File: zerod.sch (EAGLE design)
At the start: 38 parts, among them IC1 NE5532N, IC2 LM3914N, Q1 2N3906

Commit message: new, smaller board
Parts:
- renumbered C2 to C3, CY2 to C6
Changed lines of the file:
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@@
 <grid distance="0.1" unitdist="inch" unit="inch" style="lines" multiple="1" display="no" altdistance="0.01" altunitdist="inch" altunit="inch"/>
 <layers>
-<layer number="1" name="Top" color="4" fill="1" visible="yes" active="no"/>
-<layer number="16" name="Bottom" color="1" fill="1" visible="yes" active="no"/>
-<layer number="17" name="Pads" color="2" fill="1" visible="yes" active="no"/>
-<layer number="18" name="Vias" color="2" fill="1" visible="yes" active="no"/>
-<layer number="19" name="Unrouted" color="6" fill="1" visible="yes" active="no"/>
-<layer number="20" name="Dimension" color="15" fill="1" visible="yes" active="no"/>
-<layer number="21" name="tPlace" color="7" fill="1" visible="yes" active="no"/>
-<layer number="22" name="bPlace" color="7" fill="1" visible="yes" active="no"/>
-<layer number="23" name="tOrigins" color="15" fill="1" visible="yes" active="no"/>
-<layer number="24" name="bOrigins" color="15" fill="1" visible="yes" active="no"/>
-<layer number="25" name="tNames" color="7" fill="1" visible="yes" active="no"/>
-<layer number="26" name="bNames" color="7" fill="1" visible="yes" active="no"/>
-<layer number="27" name="tValues" color="7" fill="1" visible="yes" active="no"/>
-<layer number="28" name="bValues" color="7" fill="1" visible="yes" active="no"/>
+<layer number="1" name="Top" color="4" fill="1" visible="no" active="no"/>
+<layer number="16" name="Bottom" color="1" fill="1" visible="no" active="no"/>
+<layer number="17" name="Pads" color="2" fill="1" visible="no" active="no"/>
+<layer number="18" name="Vias" color="2" fill="1" visible="no" active="no"/>
+<layer number="19" name="Unrouted" color="6" fill="1" visible="no" active="no"/>
+<layer number="20" name="Dimension" color="15" fill="1" visible="no" active="no"/>
+<layer number="21" name="tPlace" color="7" fill="1" visible="no" active="no"/>
+<layer number="22" name="bPlace" color="7" fill="1" visible="no" active="no"/>
+<layer number="23" name="tOrigins" color="15" fill="1" visible="no" active="no"/>
+<layer number="24" name="bOrigins" color="15" fill="1" visible="no" active="no"/>
+<layer number="25" name="tNames" color="7" fill="1" visible="no" active="no"/>
+<layer number="26" name="bNames" color="7" fill="1" visible="no" active="no"/>
+<layer number="27" name="tValues" color="7" fill="1" visible="no" active="no"/>
+<layer number="28" name="bValues" color="7" fill="1" visible="no" active="no"/>
 <layer number="29" name="tStop" color="7" fill="3" visible="no" active="no"/>
 <layer number="30" name="bStop" color="7" fill="6" visible="no" active="no"/>
@@
 <layer number="35" name="tGlue" color="7" fill="4" visible="no" active="no"/>
 <layer number="36" name="bGlue" color="7" fill="5" visible="no" active="no"/>
-<layer number="37" name="tTest" color="7" fill="1" visible="yes" active="no"/>
-<layer number="38" name="bTest" color="7" fill="1" visible="yes" active="no"/>
+<layer number="37" name="tTest" color="7" fill="1" visible="no" active="no"/>
+<layer number="38" name="bTest" color="7" fill="1" visible="no" active="no"/>
 <layer number="39" name="tKeepout" color="4" fill="11" visible="no" active="no"/>
 <layer number="40" name="bKeepout" color="1" fill="11" visible="no" active="no"/>
@@
 <layer number="44" name="Drills" color="7" fill="1" visible="no" active="no"/>
 <layer number="45" name="Holes" color="7" fill="1" visible="no" active="no"/>
-<layer number="46" name="Milling" color="3" fill="1" visible="yes" active="no"/>
-<layer number="47" name="Measures" color="7" fill="1" visible="yes" active="no"/>
-<layer number="48" name="Document" color="7" fill="1" visible="yes" active="no"/>
-<layer number="49" name="Reference" color="7" fill="1" visible="yes" active="no"/>
-<layer number="50" name="dxf" color="7" fill="1" visible="yes" active="no"/>
-<layer number="51" name="tDocu" color="7" fill="1" visible="yes" active="no"/>
-<layer number="52" name="bDocu" color="7" fill="1" visible="yes" active="no"/>
-<layer number="53" name="tGND_GNDA" color="7" fill="9" visible="yes" active="no"/>
-<layer number="54" name="bGND_GNDA" color="1" fill="9" visible="yes" active="no"/>
-<layer number="56" name="wert" color="7" fill="1" visible="yes" active="no"/>
+<layer number="46" name="Milling" color="3" fill="1" visible="no" active="no"/>
+<layer number="47" name="Measures" color="7" fill="1" visible="no" active="no"/>
+<layer number="48" name="Document" color="7" fill="1" visible="no" active="no"/>
+<layer number="49" name="Reference" color="7" fill="1" visible="no" active="no"/>
+<layer number="50" name="dxf" color="7" fill="1" visible="no" active="no"/>
+<layer number="51" name="tDocu" color="7" fill="1" visible="no" active="no"/>
+<layer number="52" name="bDocu" color="7" fill="1" visible="no" active="no"/>
+<layer number="53" name="tGND_GNDA" color="7" fill="9" visible="no" active="no"/>
+<layer number="54" name="bGND_GNDA" color="1" fill="9" visible="no" active="no"/>
+<layer number="56" name="wert" color="7" fill="1" visible="no" active="no"/>
 <layer number="90" name="Modules" color="5" fill="1" visible="yes" active="yes"/>
 <layer number="91" name="Nets" color="2" fill="1" visible="yes" active="yes"/>
@@
 <part name="R12" library="rcl" deviceset="POTENTIOMETER_" device="PT-10S" value="5k"/>
 <part name="GND5" library="supply1" deviceset="GNDA" device=""/>
-<part name="CY2" library="rcl" deviceset="CPOL-US" device="E22-6AXIAL" value="10uF"/>
 <part name="GND7" library="supply1" deviceset="GNDA" device=""/>
 <part name="GND8" library="supply1" deviceset="GNDA" device=""/>
@@
 <part name="R3" library="rcl" deviceset="R-US_" device="0207/10" value="1k"/>
 <part name="CY3" library="rcl" deviceset="CY" device="YC7B5" value="470pF"/>
-<part name="C2" library="rcl" deviceset="CPOL-US" device="E22-6AXIAL" value="100uF"/>
 <part name="R4" library="bourns" deviceset="91" device="" value="5k"/>
 <part name="GND3" library="supply1" deviceset="GNDA" device=""/>
@@
 <part name="D2" library="diode" deviceset="1N5908" device=""/>
 <part name="D3" library="diode" deviceset="1N5908" device=""/>
+<part name="C3" library="rcl" deviceset="CPOL-US" device="E22-6AXIAL" value="100uF"/>
+<part name="C6" library="rcl" deviceset="CPOL-US" device="E22-6AXIAL" value="10uF"/>
 </parts>
 <sheets>
@@
 <instance part="R12" gate="1" x="91.44" y="12.7" rot="R90"/>
 <instance part="GND5" gate="1" x="91.44" y="-7.62"/>
-<instance part="CY2" gate="G$1" x="137.16" y="2.54"/>
 <instance part="GND7" gate="1" x="109.22" y="-7.62"/>
 <instance part="GND8" gate="1" x="137.16" y="-7.62"/>
@@
 <instance part="R3" gate="G$1" x="38.1" y="68.58" rot="R180"/>
 <instance part="CY3" gate="G$1" x="48.26" y="60.96"/>
-<instance part="C2" gate="G$1" x="83.82" y="71.12" rot="R90"/>
 <instance part="R4" gate="G$1" x="27.94" y="68.58"/>
 <instance part="IC1" gate="B" x="7.62" y="58.42"/>
@@
 <instance part="D2" gate="1" x="7.62" y="35.56" rot="R90"/>
 <instance part="D3" gate="1" x="7.62" y="22.86" rot="R90"/>
+<instance part="C3" gate="G$1" x="83.82" y="71.12" rot="R90"/>
+<instance part="C6" gate="G$1" x="137.16" y="2.54"/>
 </instances>
 <busses>
@@
 </segment>
 <segment>
-<pinref part="CY2" gate="G$1" pin="-"/>
 <pinref part="GND8" gate="1" pin="GNDA"/>
 <wire x1="137.16" y1="-2.54" x2="137.16" y2="-5.08" width="0.1524" layer="91"/>
+<pinref part="C6" gate="G$1" pin="-"/>
 </segment>
 <segment>
@@
 <wire x1="58.42" y1="83.82" x2="76.2" y2="83.82" width="0.1524" layer="91"/>
 <wire x1="76.2" y1="45.72" x2="76.2" y2="71.12" width="0.1524" layer="91"/>
-<pinref part="C2" gate="G$1" pin="+"/>
 <wire x1="76.2" y1="71.12" x2="81.28" y2="71.12" width="0.1524" layer="91"/>
+<pinref part="C3" gate="G$1" pin="+"/>
 </segment>
 </net>
@@
 <wire x1="121.92" y1="48.26" x2="121.92" y2="45.72" width="0.1524" layer="91"/>
 <wire x1="121.92" y1="45.72" x2="137.16" y2="45.72" width="0.1524" layer="91"/>
-<pinref part="CY2" gate="G$1" pin="+"/>
 <wire x1="137.16" y1="45.72" x2="137.16" y2="7.62" width="0.1524" layer="91"/>
 <pinref part="IC2" gate="A" pin="V+"/>
@@
 <wire x1="109.22" y1="45.72" x2="121.92" y2="45.72" width="0.1524" layer="91"/>
 <junction x="121.92" y="45.72"/>
+<pinref part="C6" gate="G$1" pin="+"/>
 </segment>
 <segment>
@@
 <net name="N$3" class="0">
 <segment>
-<pinref part="C2" gate="G$1" pin="-"/>
 <pinref part="R15" gate="G$1" pin="1"/>
 <wire x1="88.9" y1="71.12" x2="93.98" y2="71.12" width="0.1524" layer="91"/>
-</segment>
-</net>
+<pinref part="C3" gate="G$1" pin="-"/>
+</segment>
+</net>

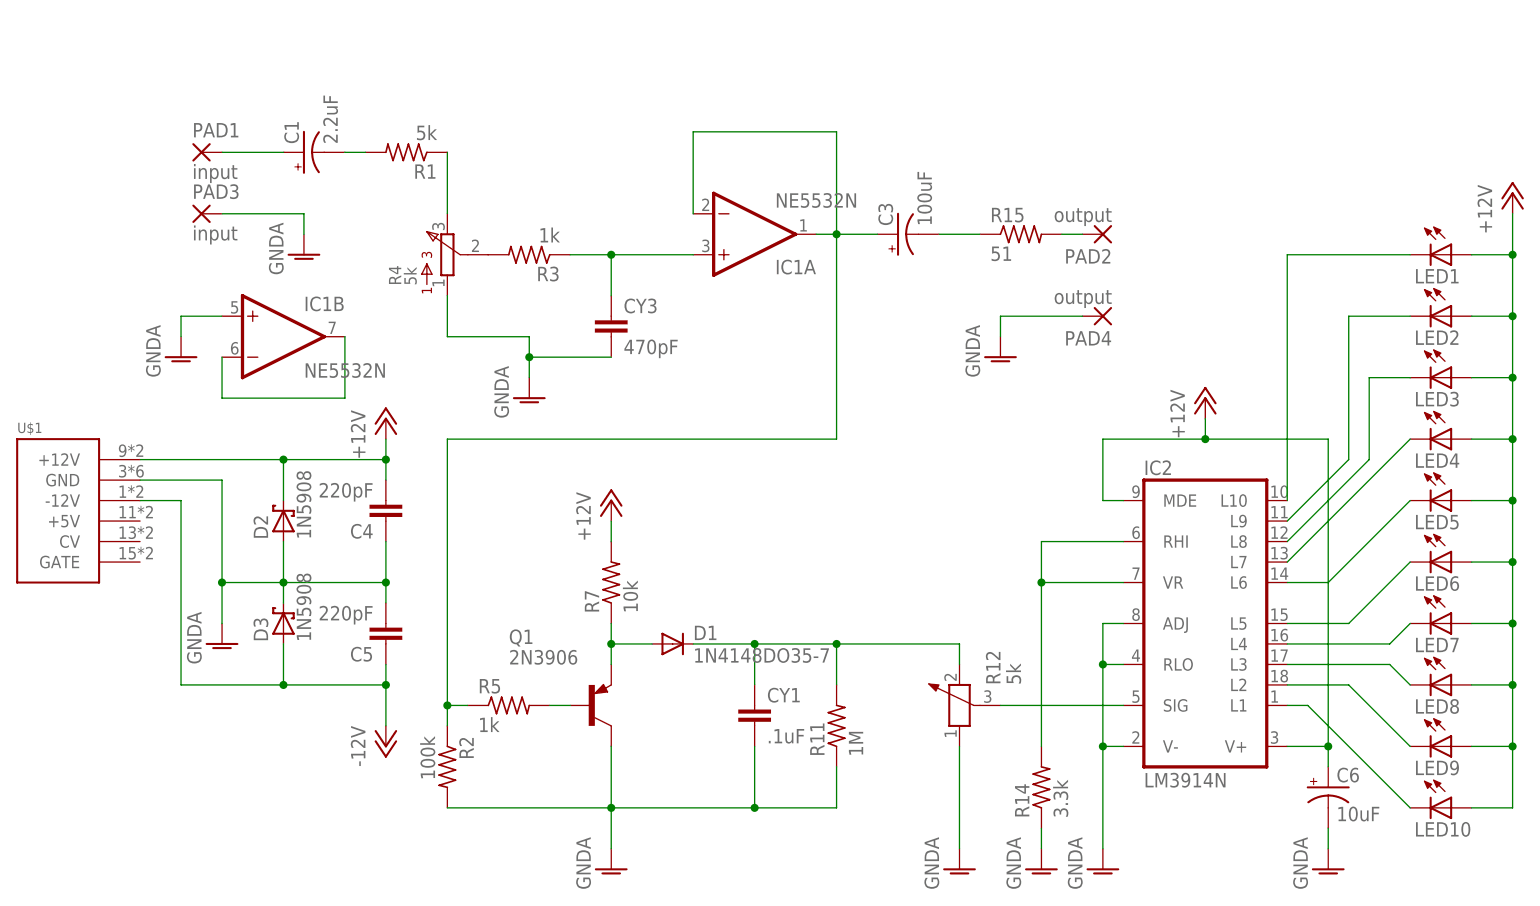
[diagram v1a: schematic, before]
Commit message: trimmer before peak detector
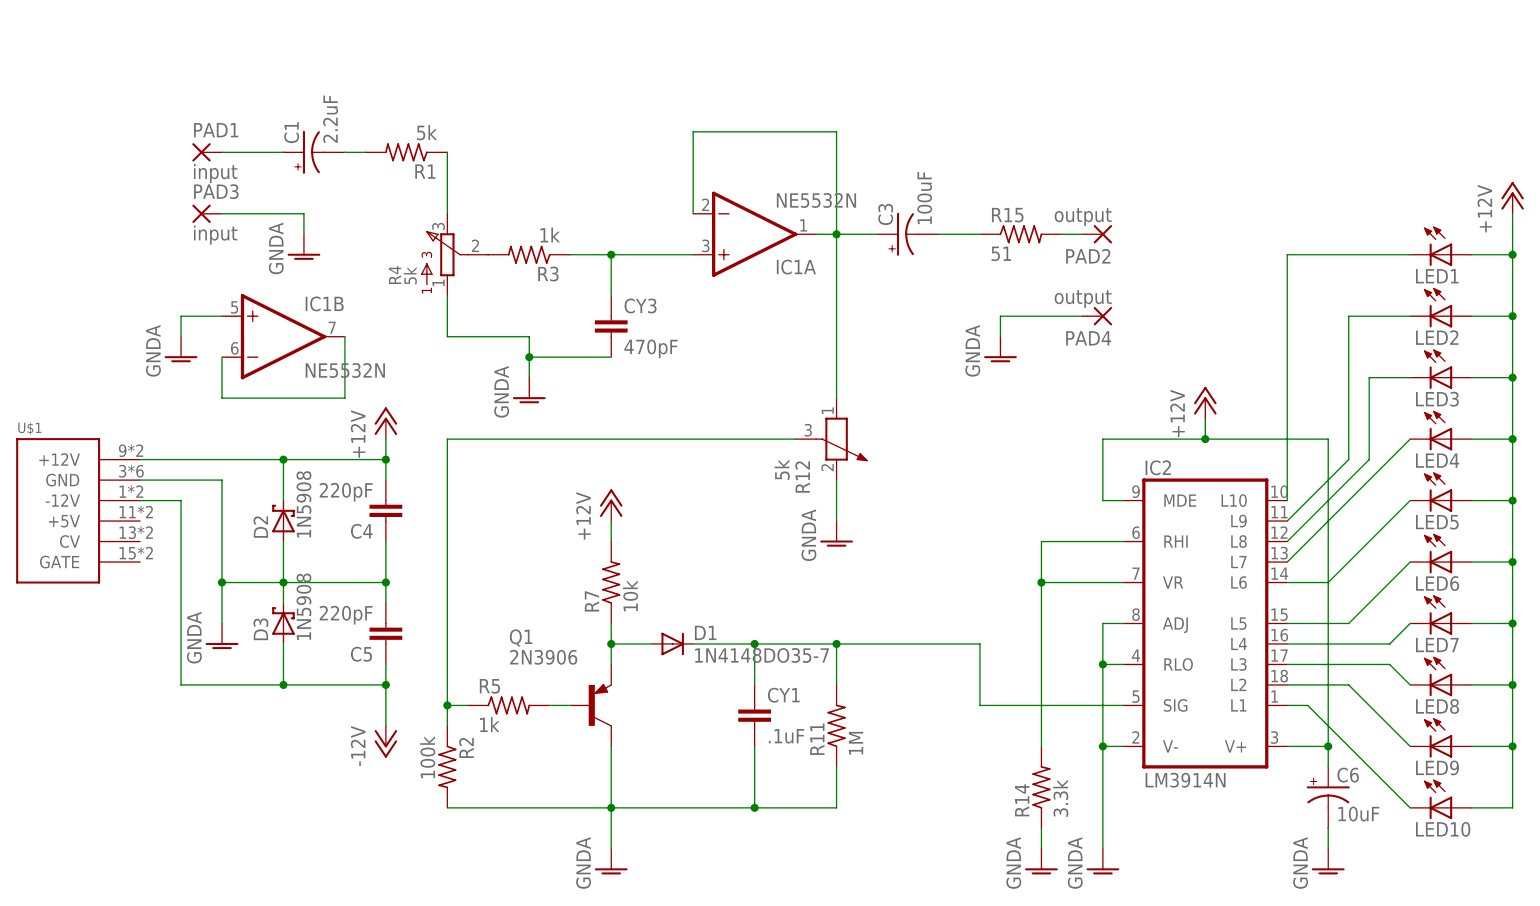
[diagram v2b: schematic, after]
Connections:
- net GNDA: now also R12.2; no longer R12.1
- net N$10: now also C3.+, IC1A.-IN, IC1A.OUT, R12.1; no longer IC2.SIG, R12.3
- net N$12: now also IC2.SIG; no longer R12.2
- net N$5: now also R12.3; no longer C3.+, IC1A.-IN, IC1A.OUT
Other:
- moved on the sheet: R12
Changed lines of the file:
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@@
 <instance part="GND2" gate="1" x="48.26" y="-7.62"/>
 <instance part="CY1" gate="G$1" x="66.04" y="12.7"/>
-<instance part="R12" gate="1" x="91.44" y="12.7" rot="R90"/>
-<instance part="GND5" gate="1" x="91.44" y="-7.62"/>
+<instance part="R12" gate="1" x="76.2" y="45.72" rot="R270"/>
+<instance part="GND5" gate="1" x="76.2" y="33.02"/>
 <instance part="GND7" gate="1" x="109.22" y="-7.62"/>
 <instance part="GND8" gate="1" x="137.16" y="-7.62"/>
@@
 </segment>
 <segment>
-<pinref part="R12" gate="1" pin="1"/>
 <pinref part="GND5" gate="1" pin="GNDA"/>
-<wire x1="91.44" y1="7.62" x2="91.44" y2="-5.08" width="0.1524" layer="91"/>
+<pinref part="R12" gate="1" pin="2"/>
+<wire x1="76.2" y1="40.64" x2="76.2" y2="35.56" width="0.1524" layer="91"/>
 </segment>
 <segment>
@@
 <wire x1="30.48" y1="12.7" x2="27.94" y2="12.7" width="0.1524" layer="91"/>
 <wire x1="27.94" y1="12.7" x2="27.94" y2="45.72" width="0.1524" layer="91"/>
-<wire x1="27.94" y1="45.72" x2="76.2" y2="45.72" width="0.1524" layer="91"/>
 <pinref part="R2" gate="G$1" pin="1"/>
 <wire x1="27.94" y1="10.16" x2="27.94" y2="12.7" width="0.1524" layer="91"/>
 <junction x="27.94" y="12.7"/>
-<pinref part="IC1" gate="A" pin="-IN"/>
-<wire x1="58.42" y1="83.82" x2="58.42" y2="73.66" width="0.1524" layer="91"/>
-<pinref part="IC1" gate="A" pin="OUT"/>
-<wire x1="73.66" y1="71.12" x2="76.2" y2="71.12" width="0.1524" layer="91"/>
-<wire x1="76.2" y1="83.82" x2="76.2" y2="71.12" width="0.1524" layer="91"/>
-<junction x="76.2" y="71.12"/>
-<wire x1="58.42" y1="83.82" x2="76.2" y2="83.82" width="0.1524" layer="91"/>
-<wire x1="76.2" y1="45.72" x2="76.2" y2="71.12" width="0.1524" layer="91"/>
-<wire x1="76.2" y1="71.12" x2="81.28" y2="71.12" width="0.1524" layer="91"/>
-<pinref part="C3" gate="G$1" pin="+"/>
+<pinref part="R12" gate="1" pin="3"/>
+<wire x1="71.12" y1="45.72" x2="27.94" y2="45.72" width="0.1524" layer="91"/>
 </segment>
 </net>
@@
 <wire x1="76.2" y1="20.32" x2="66.04" y2="20.32" width="0.1524" layer="91"/>
 <junction x="66.04" y="20.32"/>
-<wire x1="91.44" y1="20.32" x2="76.2" y2="20.32" width="0.1524" layer="91"/>
+<wire x1="93.98" y1="20.32" x2="76.2" y2="20.32" width="0.1524" layer="91"/>
 <junction x="76.2" y="20.32"/>
 <pinref part="D1" gate="G$1" pin="C"/>
 <wire x1="58.42" y1="20.32" x2="66.04" y2="20.32" width="0.1524" layer="91"/>
-<pinref part="R12" gate="1" pin="2"/>
-<wire x1="91.44" y1="20.32" x2="91.44" y2="17.78" width="0.1524" layer="91"/>
+<wire x1="93.98" y1="20.32" x2="93.98" y2="12.7" width="0.1524" layer="91"/>
+<pinref part="IC2" gate="A" pin="SIG"/>
+<wire x1="93.98" y1="12.7" x2="111.76" y2="12.7" width="0.1524" layer="91"/>
 </segment>
 </net>
@@
 </segment>
 </net>
-<net name="N$10" class="0">
-<segment>
-<pinref part="R12" gate="1" pin="3"/>
-<pinref part="IC2" gate="A" pin="SIG"/>
-<wire x1="96.52" y1="12.7" x2="111.76" y2="12.7" width="0.1524" layer="91"/>
-</segment>
-</net>
 <net name="N$14" class="0">
 <segment>
@@
 </segment>
 </net>
+<net name="N$10" class="0">
+<segment>
+<pinref part="IC1" gate="A" pin="-IN"/>
+<pinref part="C3" gate="G$1" pin="+"/>
+<pinref part="IC1" gate="A" pin="OUT"/>
+<wire x1="73.66" y1="71.12" x2="76.2" y2="71.12" width="0.1524" layer="91"/>
+<junction x="76.2" y="71.12"/>
+<wire x1="76.2" y1="71.12" x2="81.28" y2="71.12" width="0.1524" layer="91"/>
+<wire x1="76.2" y1="83.82" x2="76.2" y2="71.12" width="0.1524" layer="91"/>
+<wire x1="58.42" y1="83.82" x2="76.2" y2="83.82" width="0.1524" layer="91"/>
+<wire x1="58.42" y1="83.82" x2="58.42" y2="73.66" width="0.1524" layer="91"/>
+<pinref part="R12" gate="1" pin="1"/>
+<wire x1="76.2" y1="50.8" x2="76.2" y2="71.12" width="0.1524" layer="91"/>
+</segment>
+</net>
